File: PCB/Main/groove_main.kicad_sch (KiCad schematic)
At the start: 118 parts, among them J1 Left_X, J10 Left_Y, J11 Right_X, J12 Right_Y, J13 SW, J14 SW, J15 V, J16 LED, J17 LED, J18 G, J19 V, J2 Left_Y, J20 LED, J21 LED, J22 G, J23 SW, J24 SW, J25 V, J26 V, J27 G, J28 G, J29 HAP, J3 Right_X, J30 V, J31 HAP, J32 V, J4 Right_Y, J5 Left_X, J6 Left_Y, J7 Right_X, J8 Right_Y, J9 Left_X, Q1 AO3400A, Q2 AO3400A, SW1 SWITCH_SPST, SW2 SWITCH_SPST, SW3 SWITCH_SPST, SW4 SWITCH_SPST, SW5 SWITCH_SPST, U1 PiPico, U2 CD4052B, U3 LM4040DBZ-3

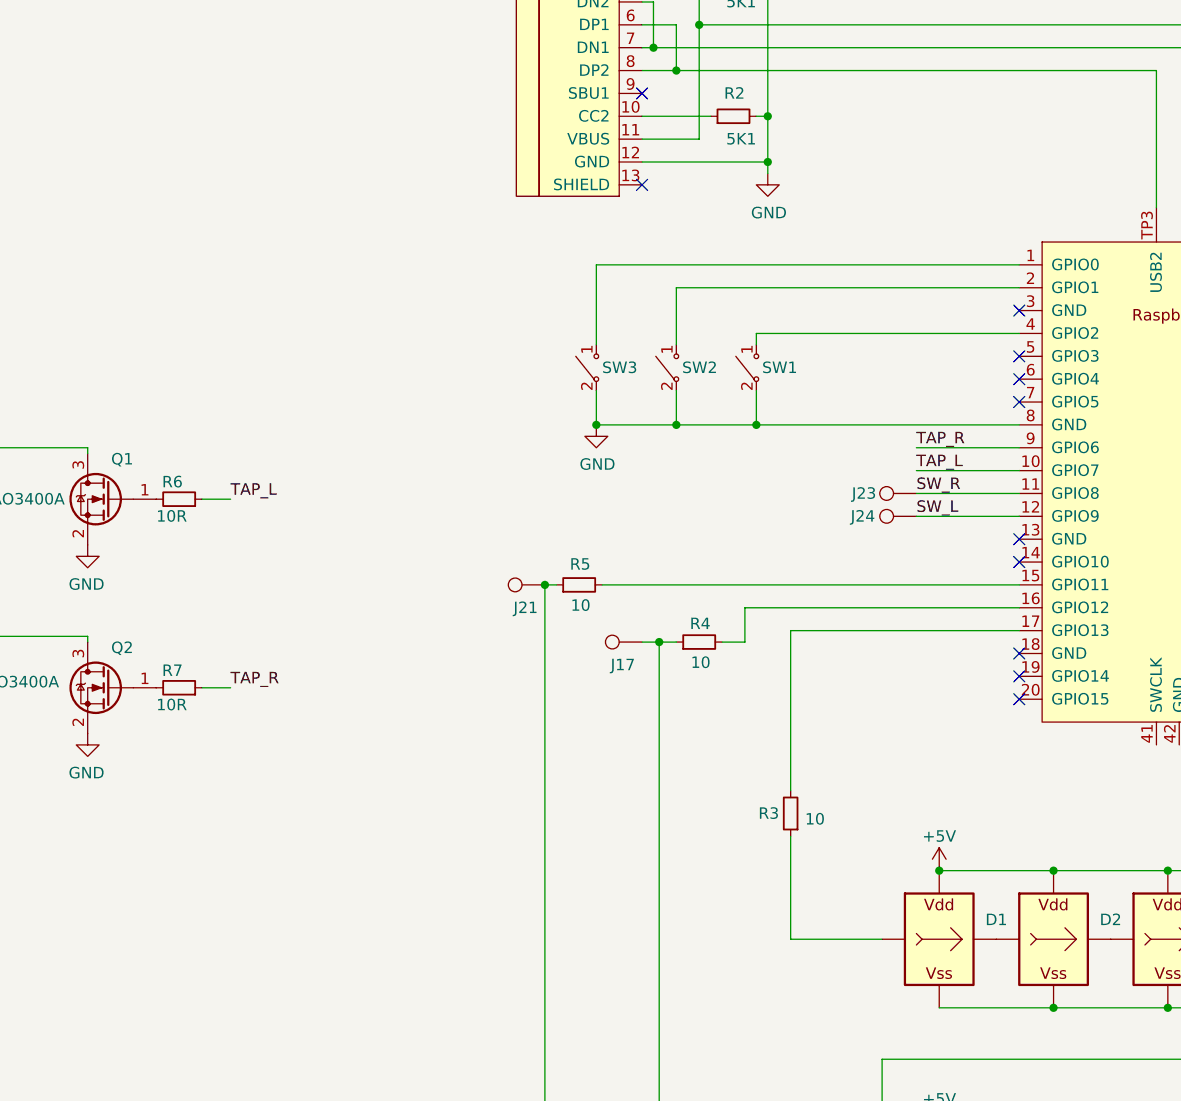
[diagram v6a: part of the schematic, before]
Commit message: PCB v1.21 (easier soldering)
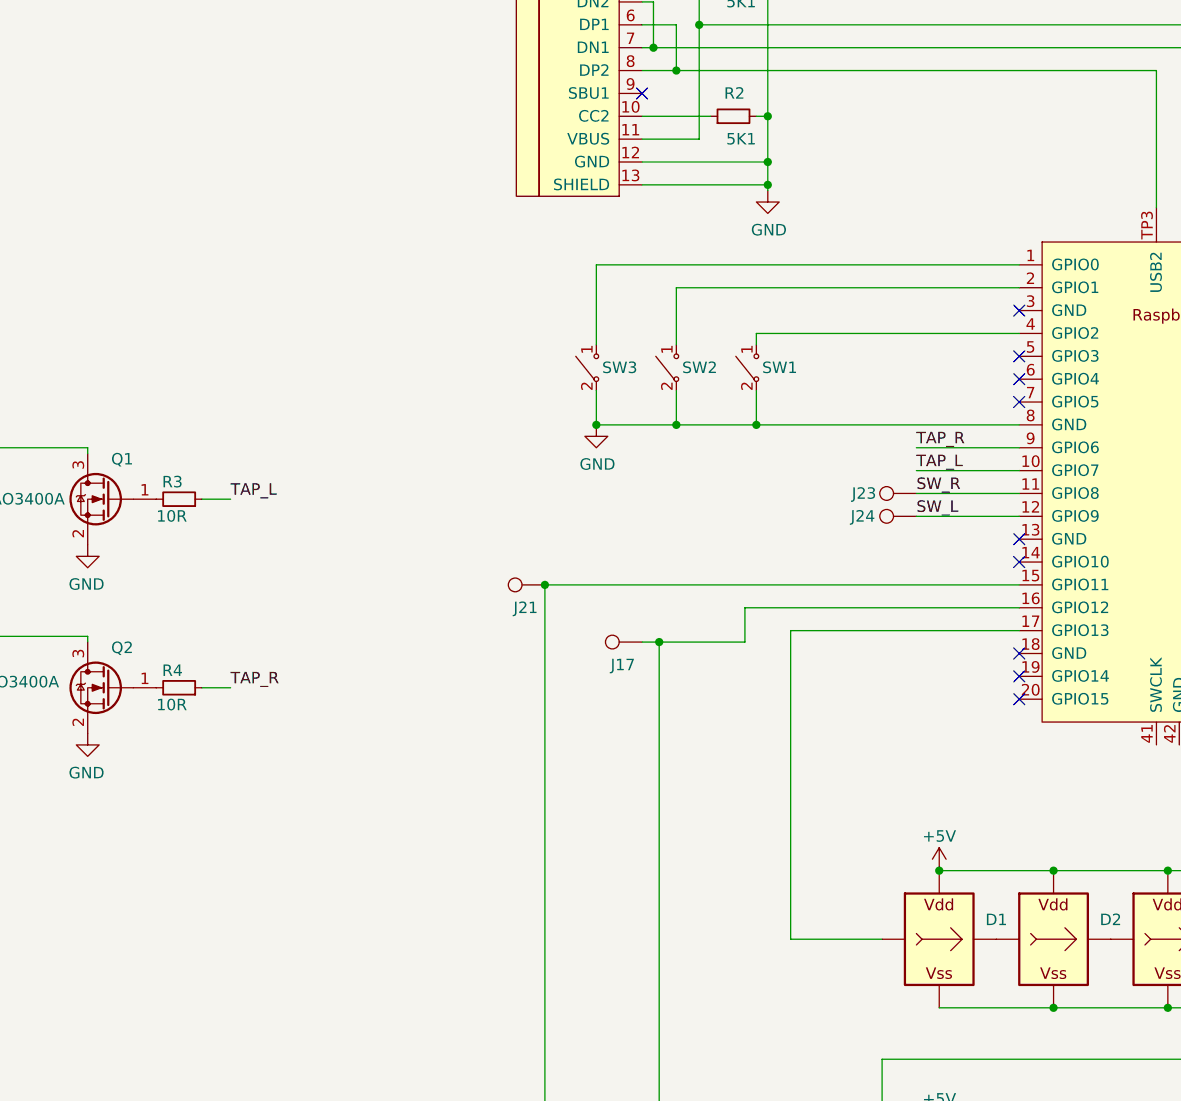
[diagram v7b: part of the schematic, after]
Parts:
- removed R3, R4, R5: 10, Resistor_SMD:R_0603_1608Metric, symbol Device:R_Small
- R1, R2: footprint Resistor_SMD:R_0603_1608Metric -> Resistor_SMD:R_0603_1608Metric_Pad0.98x0.95mm_HandSolder
- R3: renamed from R6; footprint Resistor_SMD:R_0603_1608Metric -> Resistor_SMD:R_0603_1608Metric_Pad0.98x0.95mm_HandSolder
- R4: renamed from R7; footprint Resistor_SMD:R_0603_1608Metric -> Resistor_SMD:R_0603_1608Metric_Pad0.98x0.95mm_HandSolder
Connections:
- net GND: now also USB1.13 (SHIELD)
- net at D20.I (In), J16.1, J17.1: now also U1.16 (GPIO12)
- net at D32.I (In), J20.1, J21.1: now also U1.15 (GPIO11)
- net at D1.I (In): now also U1.17 (GPIO13)
- no-connect marks 23 -> 22

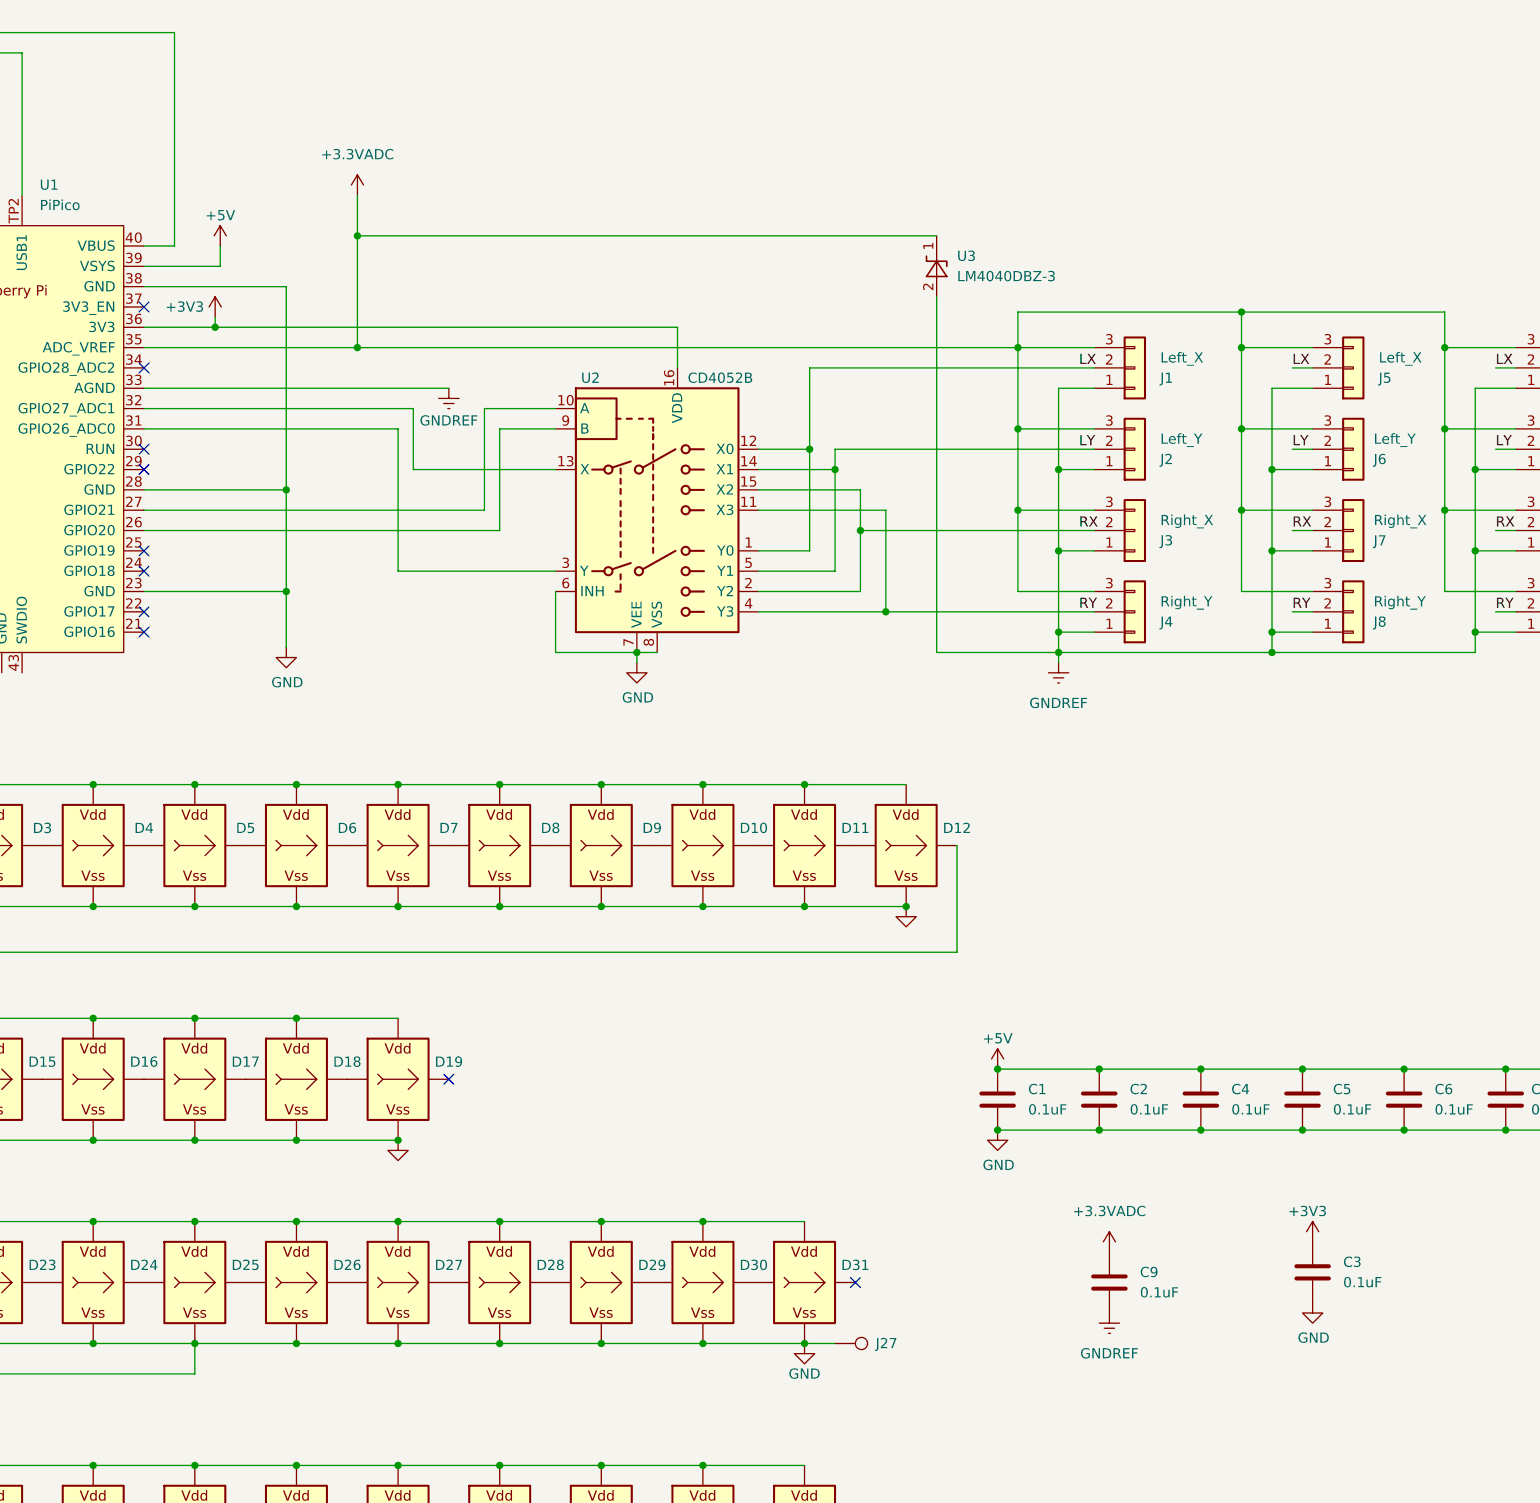
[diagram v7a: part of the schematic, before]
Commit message: Improve voltage reference design
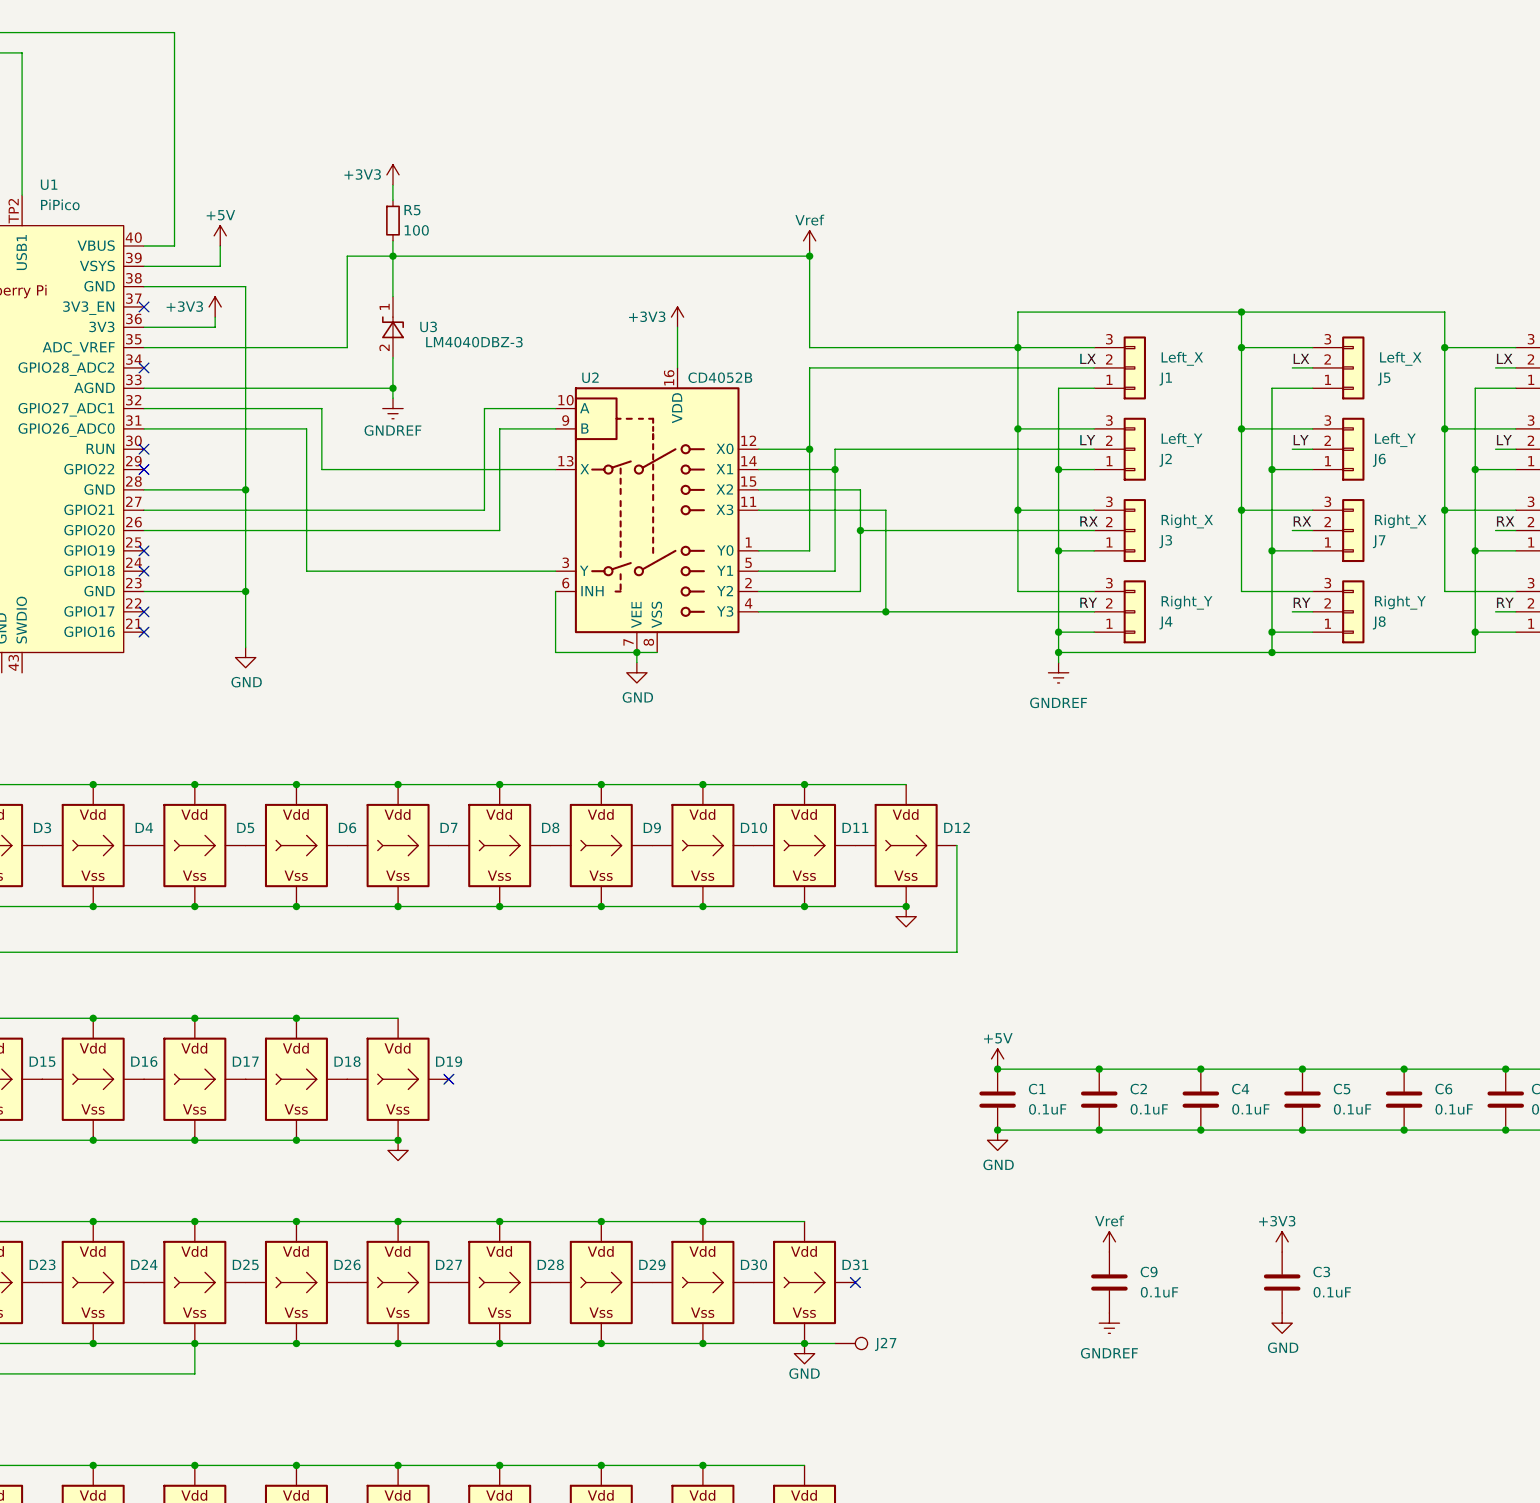
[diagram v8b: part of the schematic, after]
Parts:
- added R5: 100, Resistor_SMD:R_0603_1608Metric_Pad0.98x0.95mm_HandSolder, symbol Device:R_Small
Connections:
- net +3V3: now also R5.1
- net +3.3VADC renamed Vref
- net Vref: now also R5.2
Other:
- moved on the sheet: C3, U3
